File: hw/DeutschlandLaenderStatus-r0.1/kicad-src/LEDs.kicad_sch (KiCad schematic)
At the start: 16 parts

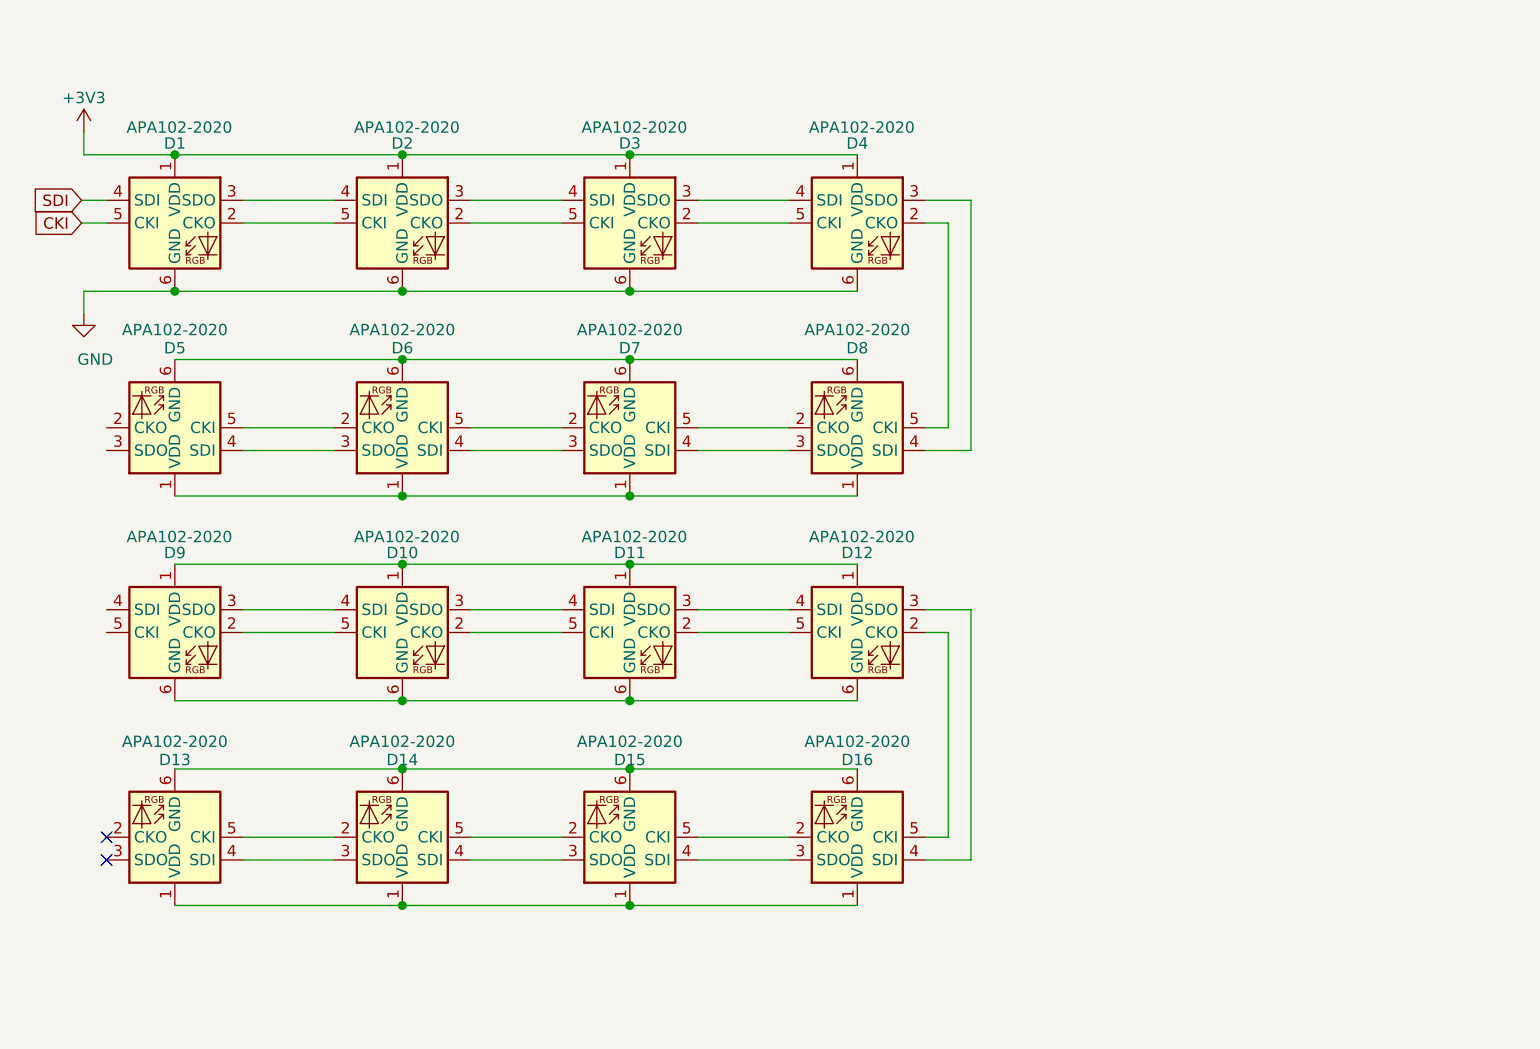
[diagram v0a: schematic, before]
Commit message: added 7segment display
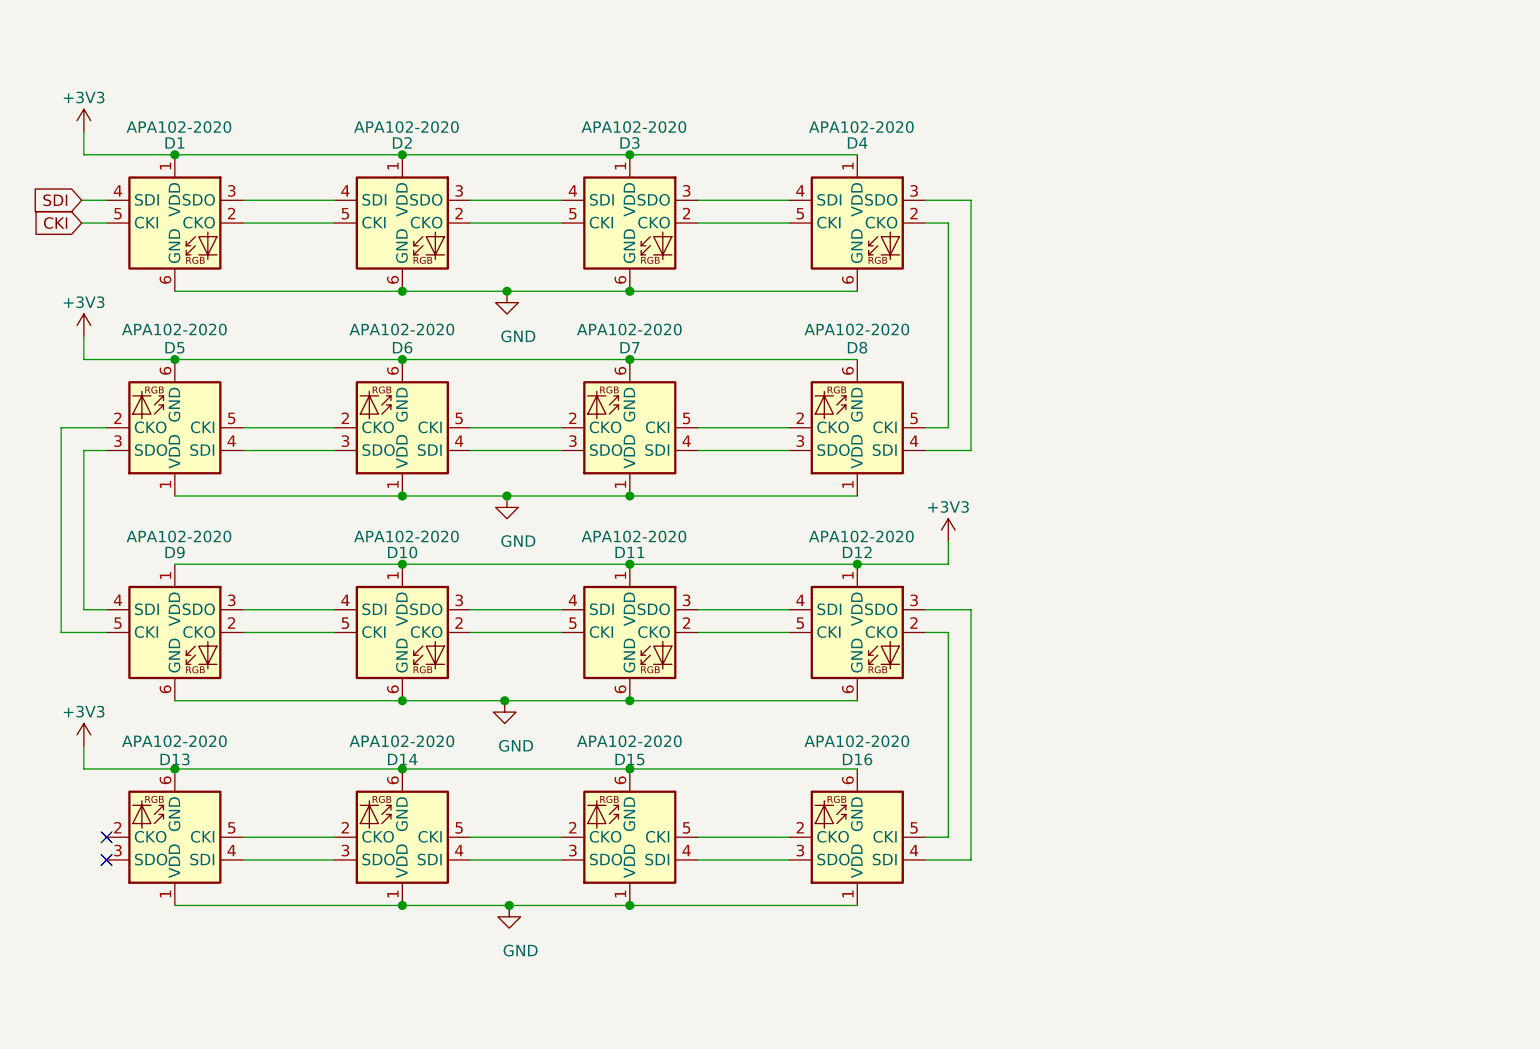
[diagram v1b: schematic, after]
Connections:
- net +3V3: now also D10.1 (VDD), D11.1 (VDD), D12.1 (VDD), D13.6 (GND), D14.6 (GND), D15.6 (GND), D16.6 (GND), D5.6 (GND), D6.6 (GND), D7.6 (GND), D8.6 (GND), D9.1 (VDD)
- net GND: now also D10.6 (GND), D11.6 (GND), D12.6 (GND), D13.1 (VDD), D14.1 (VDD), D15.1 (VDD), D16.1 (VDD), D5.1 (VDD), D6.1 (VDD), D7.1 (VDD), D8.1 (VDD), D9.6 (GND)
- net at D9.4 (SDI): now also D5.3 (SDO)
- net at D9.5 (CKI): now also D5.2 (CKO)

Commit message: Layout complete
Need to added Map Outline still
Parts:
- added C18, C19: 100n, Capacitor_SMD:C_0402_1005Metric, symbol icebreaker-bitsy-rescue:pkl_C_Small-pkl_device
- added U10: SN74LVC2T45DCUR, Package_SO:VSSOP-8_2.4x2.1mm_P0.5mm, symbol Logic_LevelTranslator:SN74LVC2T45DCUR
- D1, D10, D11, D12, D13, D14, D15, D16, D2, D3, D4, D5, D6, D7, D8, D9: footprint LED_SMD:LED-APA102-2020 -> kt-footprints:LED-APA102-2020
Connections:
- net +3V3: now also C18.1, U10.8 (VCCB); no longer D1.1 (VDD), D10.1 (VDD), D11.1 (VDD), D12.1 (VDD), D13.6 (GND), D14.6 (GND), D15.6 (GND), D16.6 (GND), D2.1 (VDD), D3.1 (VDD), D4.1 (VDD), D5.6 (GND), D6.6 (GND), D7.6 (GND), D8.6 (GND), D9.1 (VDD)
- net CKI: now also U10.6 (B2); no longer D1.5 (CKI)
- net GND: now also D13.6 (GND), D14.6 (GND), D15.6 (GND), D16.6 (GND), D5.6 (GND), D6.6 (GND), D7.6 (GND), D8.6 (GND), C18.2, C19.2, U10.4 (GND), U10.5 (DIR); no longer D13.1 (VDD), D14.1 (VDD), D15.1 (VDD), D16.1 (VDD), D5.1 (VDD), D6.1 (VDD), D7.1 (VDD), D8.1 (VDD)
- net SDI: now also U10.7 (B1); no longer D1.4 (SDI)
- net at D14.2 (CKO): now also D15.5 (CKI); no longer D13.5 (CKI)
- net at D14.3 (SDO): now also D15.4 (SDI); no longer D13.4 (SDI)
- net at D14.4 (SDI): now also D13.3 (SDO); no longer D15.3 (SDO)
- net at D14.5 (CKI): now also D13.2 (CKO); no longer D15.2 (CKO)
- net at D4.2 (CKO): now also D5.5 (CKI); no longer D8.5 (CKI)
- net at D4.3 (SDO): now also D5.4 (SDI); no longer D8.4 (SDI)
- net at D7.2 (CKO): now also D8.5 (CKI); no longer D6.5 (CKI)
- net at D7.3 (SDO): now also D8.4 (SDI); no longer D6.4 (SDI)
- net at D7.4 (SDI): now also D6.3 (SDO); no longer D8.3 (SDO)
- net at D7.5 (CKI): now also D6.2 (CKO); no longer D8.2 (CKO)
- net at D12.2 (CKO): now also D13.5 (CKI); no longer D16.5 (CKI)
- net at D12.3 (SDO): now also D13.4 (SDI); no longer D16.4 (SDI)
- net at D9.4 (SDI): now also D8.3 (SDO); no longer D5.3 (SDO)
- net at D9.5 (CKI): now also D8.2 (CKO); no longer D5.2 (CKO)
- net at D16.2 (CKO): no longer D15.5 (CKI)
- net at D16.3 (SDO): no longer D15.4 (SDI)
- new net: D1.4 (SDI), U10.2 (A1)
- new net: D1.5 (CKI), U10.3 (A2)
- new net: D15.3 (SDO), D16.4 (SDI)
- new net: D15.2 (CKO), D16.5 (CKI)
- new net: D5.2 (CKO), D6.5 (CKI)
- new net: D5.3 (SDO), D6.4 (SDI)
- new net VBUS: C19.1, D1.1 (VDD), D10.1 (VDD), D11.1 (VDD), D12.1 (VDD), D13.1 (VDD), D14.1 (VDD), D15.1 (VDD), D16.1 (VDD), D2.1 (VDD), D3.1 (VDD), D4.1 (VDD), D5.1 (VDD), D6.1 (VDD), D7.1 (VDD), D8.1 (VDD), D9.1 (VDD), U10.1 (VCCA)
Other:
- moved on the sheet: D1, D10, D11, D12, D13, D14, D15, D16, D2, D3, D4, D5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
